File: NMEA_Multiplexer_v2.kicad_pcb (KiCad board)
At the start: 2 copper layers, 65 x 45 mm, 94 parts, among them J1 USB, J2 PoRt 1, J3 PoRt 2, J4 PoRt 3, J5 PoRt 4, J6 PoRt 5, J7 12V, J8 DEBUG UART, J9 JTAG, SW1 Reset, U1 ATSAMG55J19A-AU, U2 XR32330, U3 XR32330, U4 LF33ABDT-TR, U5 HM-11, Y1 32.768k

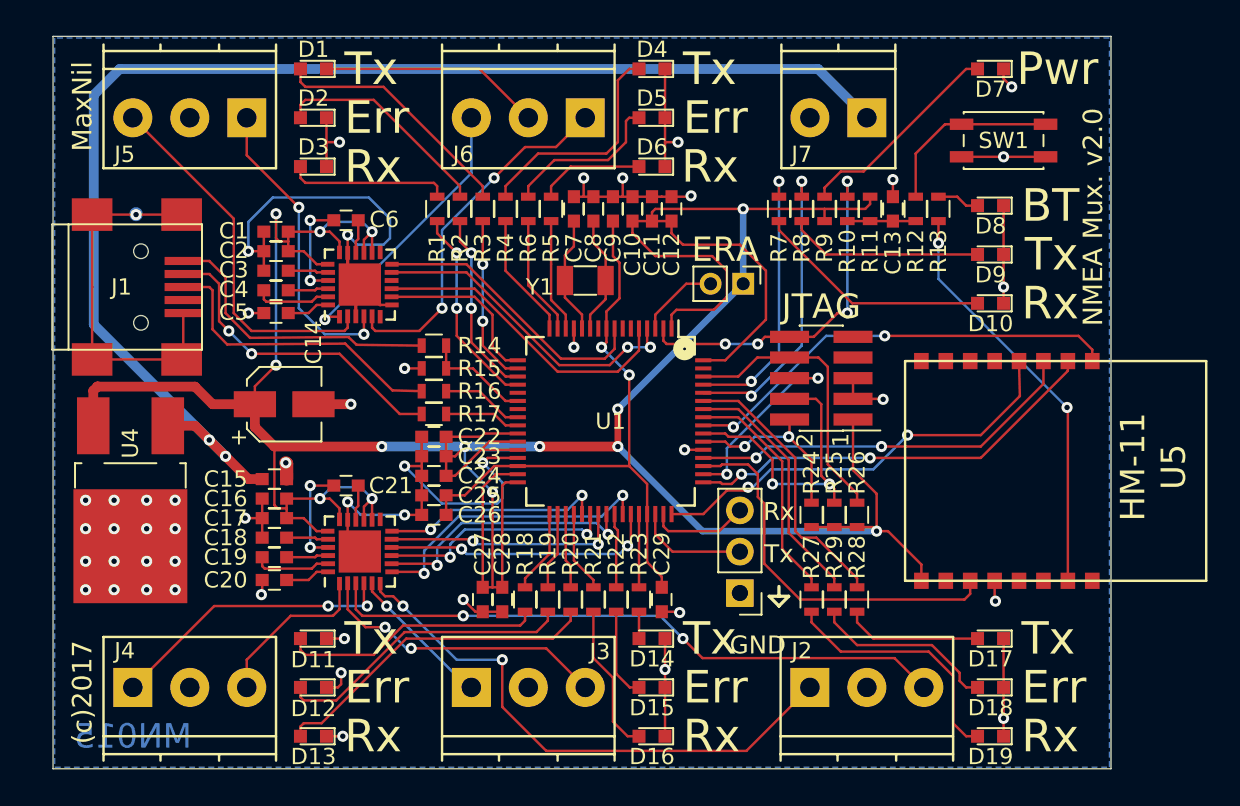
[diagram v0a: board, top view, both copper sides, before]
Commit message: Updated USB footprint Connected BT KEY pin
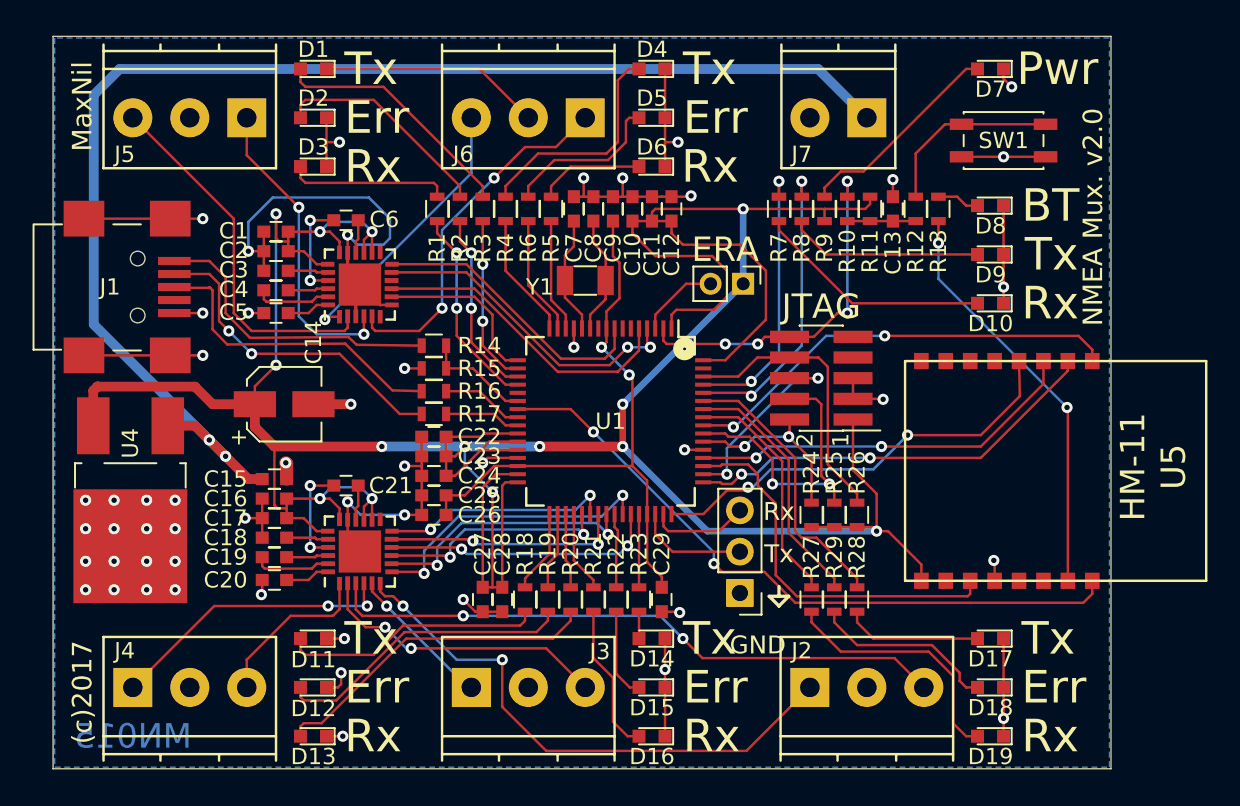
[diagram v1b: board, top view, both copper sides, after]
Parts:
- D1: value Tx 3 (gReen) -> Tx 3 (green)
- D11: value Tx (gReen) -> Tx (green)
- D12: value ERr 2 (reD) -> Err 2 (red)
- D14: value Tx 1 (gReen) -> Tx 1 (green)
- D15: value ERr 1 (reD) -> Err 1 (red)
- D17: value Tx 0 (gReen) -> Tx 0 (green)
- D18: value ERr 0 (reD) -> Err 0 (red)
- D2: value ERr 3 (reD) -> Err 3 (red)
- D4: value Tx 4 (gReen) -> Tx 4 (green)
- D5: value ERr 4 (reD) -> Err 4 (red)
- D8: value BT Cxon (blue) -> BT Con (blue)
- D9: value Tx BT (gReen) -> Tx BT (green)
- J1: footprint Connectors:USB_Mini-B -> MaxNil:USB_Mini-B_UX60-MB-5ST
- J2: value PoRt 1 -> Port 1
- J3: value PoRt 2 -> Port 2
- J4: value PoRt 3 -> Port 3
- J5: value PoRt 4 -> Port 4
- J6: value PoRt 5 -> Port 5
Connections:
- net /LED_BT_CxON renamed /LED_BT_CON
- J2 pad 1: /TX2 -> /TX0
- J2 pad 3: /RX2 -> /RX0
- J4 pad 1: /TX0 -> /TX2
- J4 pad 3: /RX0 -> /RX2
- U1 pad 23: Net-(U1-Pad23) -> /BT_KEY
- U1 pad 37: /RXD6 -> /TXD6
- U1 pad 38: /TXD6 -> /RXD6
- U3 pad 1: /RX0 -> /RX2
- U3 pad 3: /RX2 -> /RX0
- U3 pad 4: /TX0 -> /TX2
- U3 pad 6: /TX2 -> /TX0
- U5 pad 16: Net-(U5-Pad16) -> /BT_KEY
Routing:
- net /BT_KEY: track 0.00 -> 41.7 mm, vias 0 -> 2
- net /RX2: track 38.5 -> 10.3 mm, vias 2 -> 0
- net /RX0: track 10.3 -> 38.5 mm, vias 0 -> 2
- net /TX2: track 34.2 -> 18.0 mm
- net /TX0: track 18.0 -> 34.2 mm
- net GND: track 174.9 -> 158.8 mm, vias 49 -> 51
- net Net-(J1-Pad3): track 18.7 -> 19.3 mm
- net Net-(J1-Pad1): track 18.1 -> 18.6 mm
- net Net-(J1-Pad2): track 19.6 -> 20.1 mm
- net /RXD6: track 13.7 -> 14.2 mm
